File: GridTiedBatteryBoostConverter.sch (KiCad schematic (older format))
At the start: 58 parts, among them J101 Battery Connection, J103 Solar Panels, Q101 IXFP36N20X3, Q102 BC847B-13-F, Q103 SSM3K329R, Q104 SSM3J334R, U101 OPA2837DGK, U102 UCC2800DTR

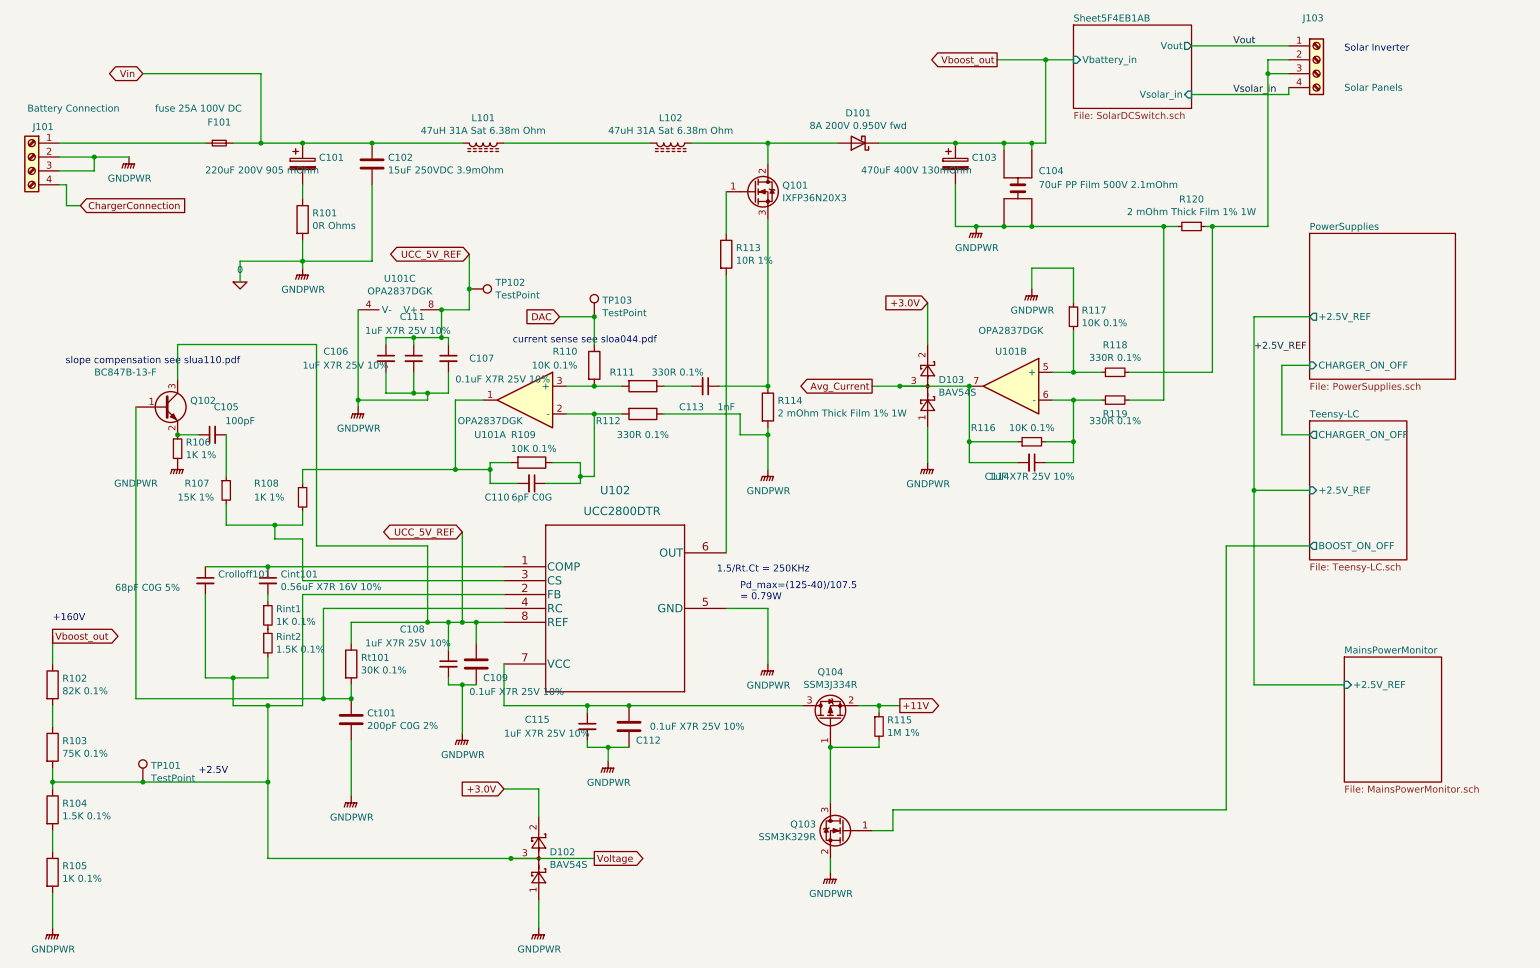
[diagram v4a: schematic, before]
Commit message: Finished adding digi key part numbers, for now git add *
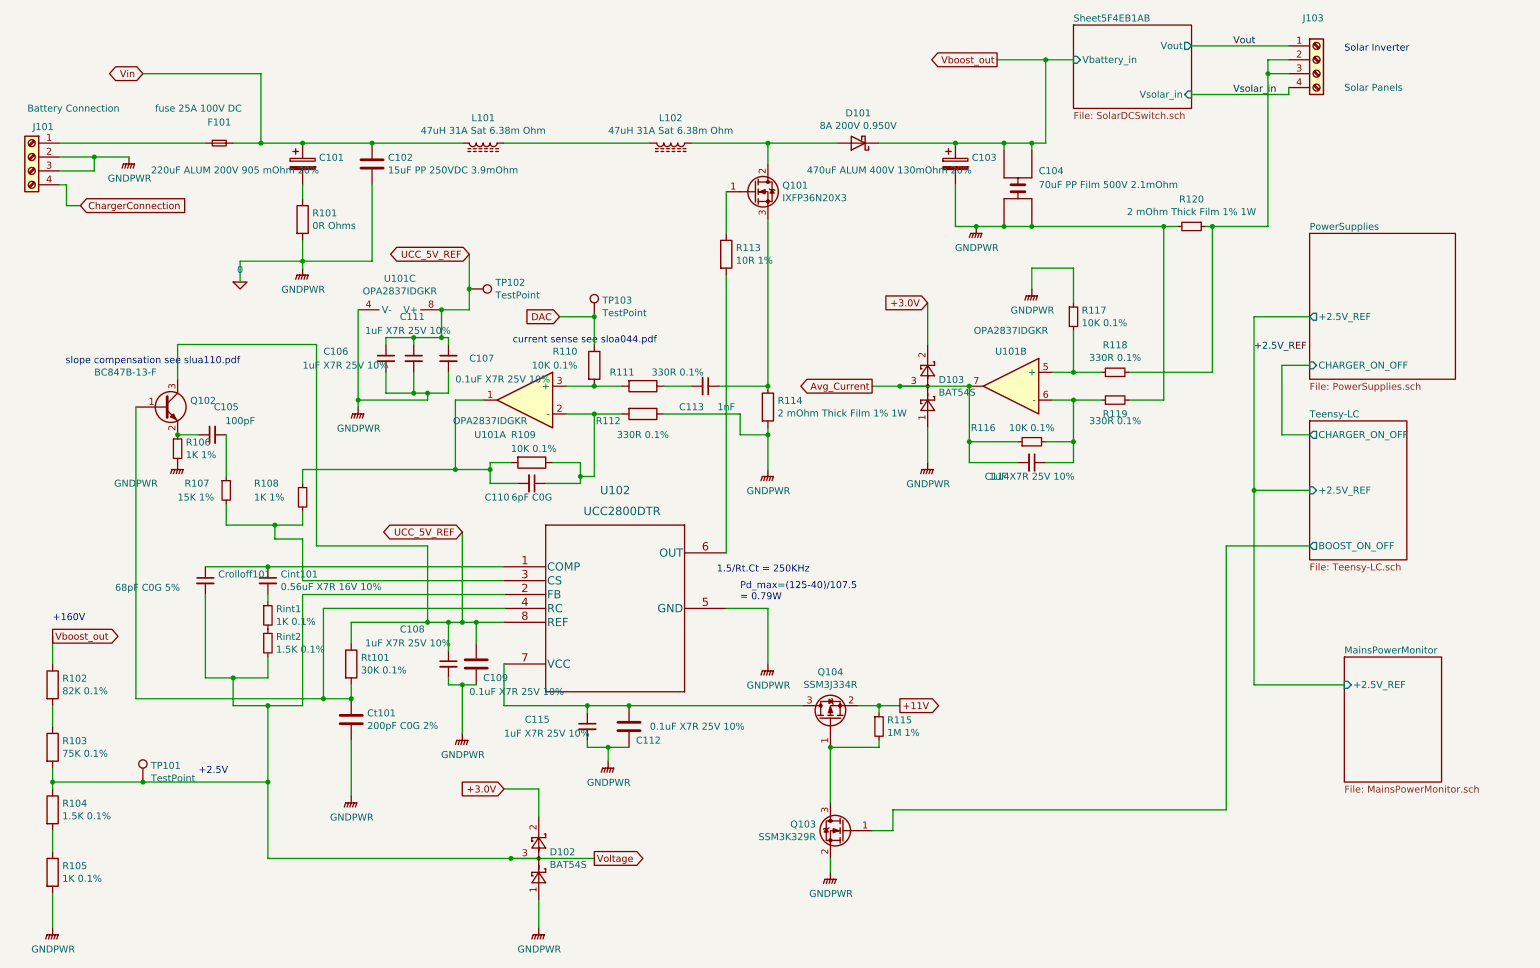
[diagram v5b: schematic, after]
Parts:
- C101: value 220uF 200V 905 mOhm -> 220uF ALUM 200V 905 mOhm 20%; MFR - -> Cornell Dubilier Electronics (CDE); MPN - -> SLP221M200A1P3; SPN - -> 338-1478-ND; SPR - -> digikey
- C102: value 15uF 250VDC 3.9mOhm -> 15uF PP 250VDC 3.9mOhm; MFR - -> KEMET; MPN - -> C4GADUD5150AA1J; SPN - -> 399-13088-ND; SPR - -> digikey
- C103: value 470uF 400V 130mOhm -> 470uF ALUM 400V 130mOhm 20%; MFR - -> KEMET; MPN - -> ELH477M400AT4AA; SPN - -> 399-6073-ND; SPR - -> digikey
- C104: MFR - -> KEMET; MPN - -> C4AQLBW5700A3LK; SPN - -> 399-17006-ND; SPR - -> digikey
- D101: value 8A 200V 0.950V fwd -> 8A 200V 0.950V; MFR - -> Vishay Semiconductor Diodes Division; MPN - -> FES8DT-E3/45; SPN - -> FES8DT-E3/45GI-ND; SPR - -> digikey
- D102, D103: value BAV54S -> BAT54S; MFR - -> Toshiba Semiconductor and Storage; MPN - -> TBAT54S,LM; SPN - -> TBAT54SLMCT-ND; SPR - -> digikey
- F101: MFR - -> Schurter Inc; MPN - -> SUT-H-6332-25A00-CTG-TT-NI; SPN - -> 486-7266-ND; SPR - -> digikey
- J101: MFR - -> Phoenix Contact; MPN - -> 1935792; SPN - -> 277-14426-ND; SPR - -> digikey
- J103: MFR - -> Phoenix Contact; MPN - -> 1017516; SPN - -> 277-17506-ND; SPR - -> digikey
- L101, L102: MFR - -> Wurth Elektronik; MPN - -> 7443763540470; SPN - -> 732-13644-ND; SPR - -> digikey
- Q101: MFR - -> IXYS; MPN - -> IXFP36N20X3; SPN - -> IXFP36N20X3-ND; SPR - -> digikey
- Q102: MFR - -> Diodes Incorporated; MPN - -> BC847B-13-F; SPN - -> BC847B-13-FDICT-ND; SPR - -> digikey
- Q103: MFR - -> Toshiba Semiconductor and Storage; MPN - -> SSM3K329R,LF; SPN - -> SSM3K329RLFCT-ND; SPR - -> digikey
- Q104: MFR - -> Toshiba Semiconductor and Storage; MPN - -> SSM3J334R,LF; SPN - -> SSM3J334RLFCT-ND; SPR - -> digikey
- U101: value OPA2837DGK -> OPA2837IDGKR; MFR - -> Texas Instruments; MPN - -> OPA2837IDGKR; SPN - -> 296-49464-1-ND; SPR - -> digikey
- U102: MFR - -> Texas Instruments; MPN - -> UCC2800DTR; SPN - -> 296-39529-1-ND; SPR - -> digikey

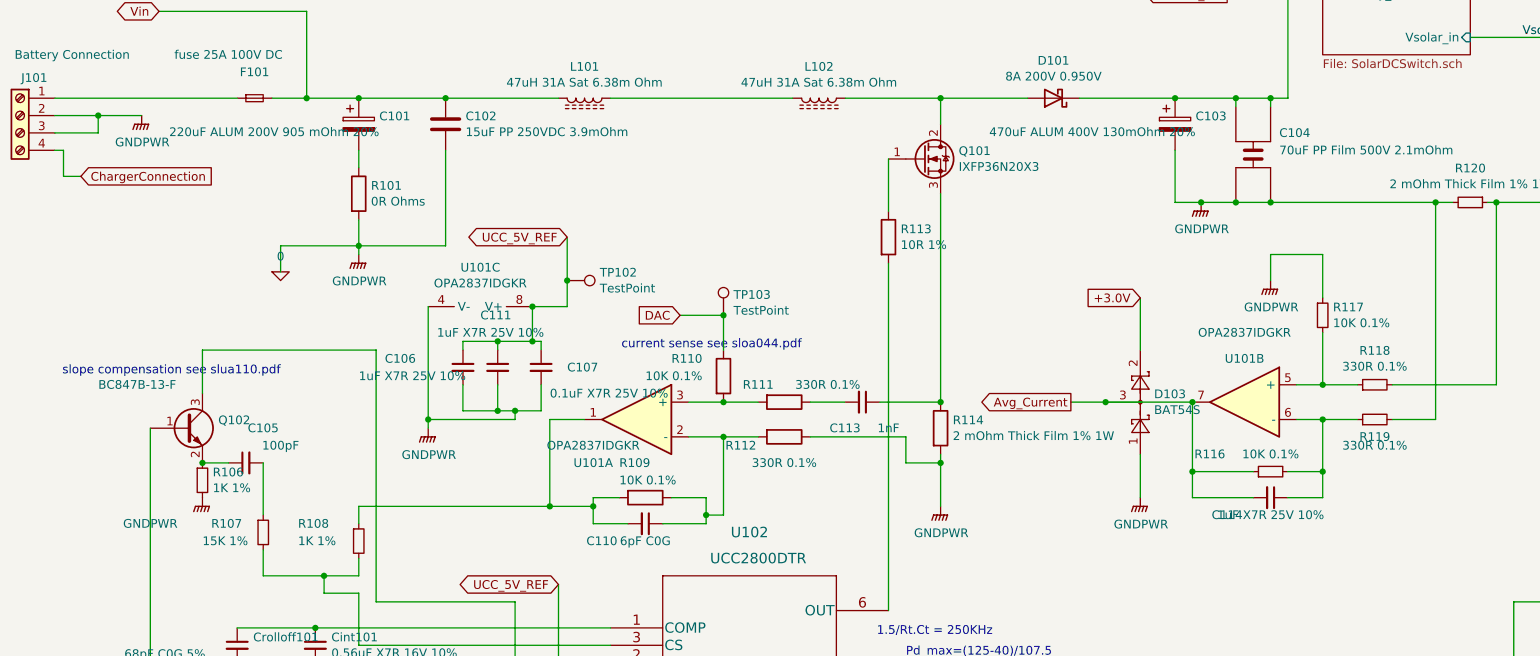
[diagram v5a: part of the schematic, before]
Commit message: added thermal via of .3 drill size and .6, I have read the recomenned size is .25 drill but the smallest JLCPCB do for double sided boards is .3
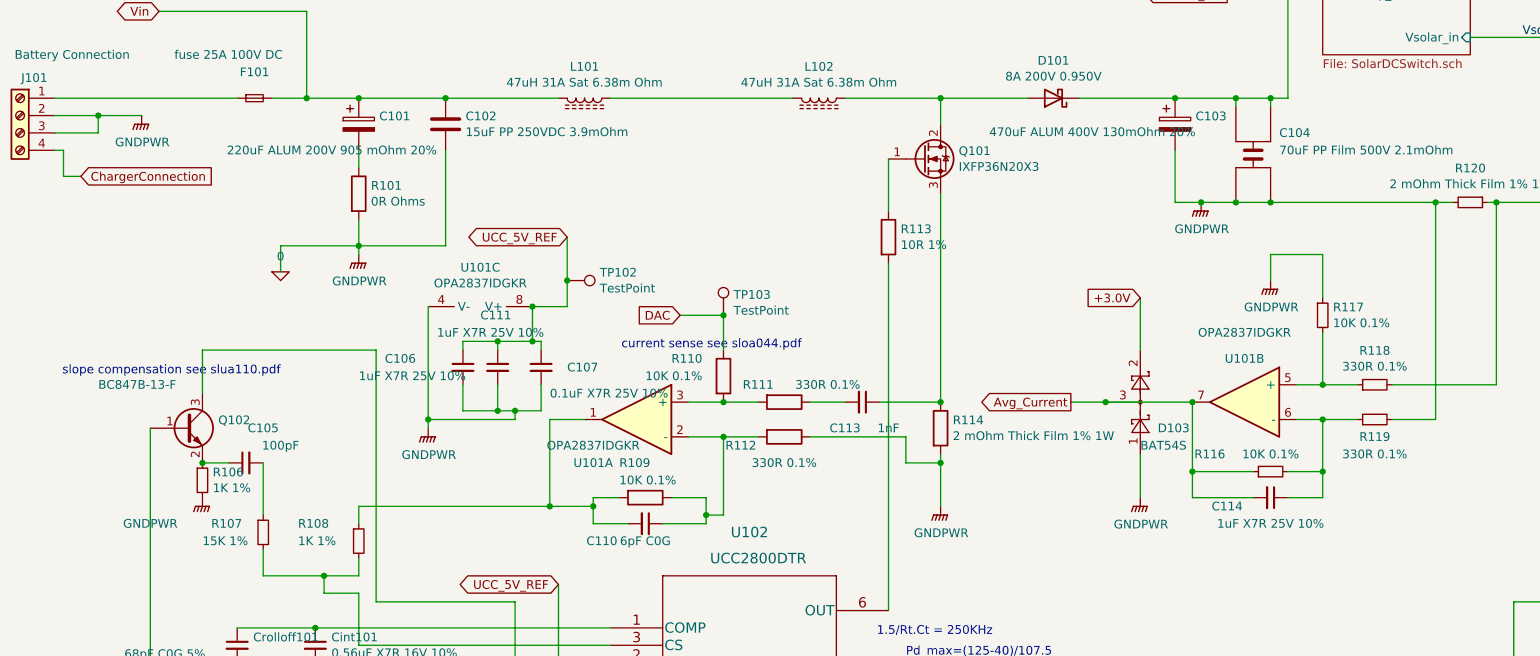
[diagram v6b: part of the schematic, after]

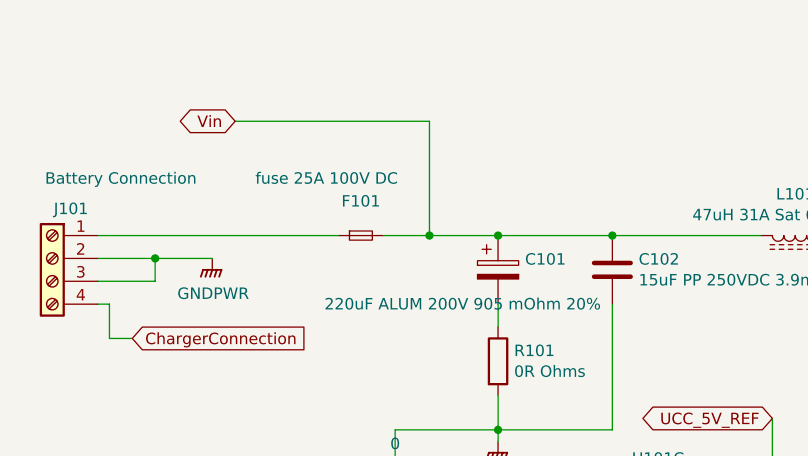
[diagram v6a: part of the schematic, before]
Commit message: change Fuse details to a graphic note, and change the Fuse supply details to refer to the fuse holder, not the fuse it self.  Also rerouted the charger input using 8mm trace width were possible.
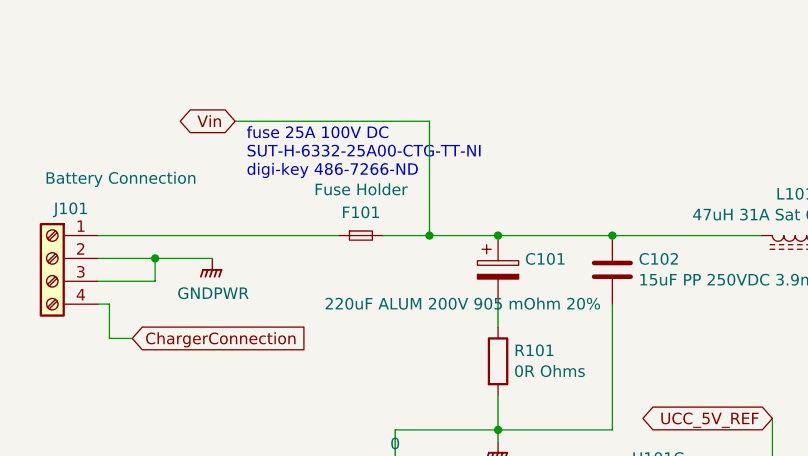
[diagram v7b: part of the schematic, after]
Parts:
- F101: value fuse 25A 100V DC -> Fuse Holder; MFR Schurter Inc -> Bel Fuse Inc.; MPN SUT-H-6332-25A00-CTG-TT-NI -> FC-102-22; SPN 486-7266-ND -> 507-1702-ND
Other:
- note added: "fuse 25A 100V DC\nSUT-H-6332-25A00-CTG-TT-NI\ndigi-key 486-7266-ND"

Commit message: Started making progress towards people being able to clone the the repository without getting messages about missing librarys needing rescue. started simplifying where some component librarys are located.
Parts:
- U101: symbol 2020-03-11_04-11-57:OPA2837DGK -> TI:OPA2837DGK
- U102: symbol UCC2800DTR:UCC2800DTR -> TI:UCC2800DTR
